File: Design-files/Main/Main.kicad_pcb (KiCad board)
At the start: 2 copper layers, 25 parts, among them J1 USB_B_Micro, J2 Conn_01x02_Pin, J3 Conn_01x24_Pin, J4 Conn_01x24_Socket, J5 Conn_01x24_Socket, J6 Conn_01x24_Pin, J7 Conn_01x10_Pin, U1 CH340C, U2 CAT24C256, U3 HT75xx-1-SOT89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

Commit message: changes
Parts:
- added C5: 1 uF, Capacitor_SMD:C_0201_0603Metric, F.Cu at (136.9, 52.9)
- added C6: 1 uF, Capacitor_SMD:C_0201_0603Metric, F.Cu at (136.9, 54.6)
- added C7: 10 uF, Capacitor_SMD:C_0201_0603Metric, F.Cu at (220.6, 55.9)
- added C8: 0.1uF, Capacitor_SMD:C_0201_0603Metric, F.Cu at (173.1, 116.8)
- added C9: 0.1uF, Capacitor_SMD:C_0201_0603Metric, F.Cu at (175.3, 99.1)
- added J13: Conn_01x02_Pin, Connector_PinHeader_2.54mm:PinHeader_1x02_P2.54mm_Vertical, F.Cu at (182.9, 68.6)
- added J8: Conn_01x04_Pin, Connector_PinHeader_2.54mm:PinHeader_1x04_P2.54mm_Vertical, F.Cu at (177.8, 68.6)
- added J9: Conn_01x02_Pin, Connector_PinHeader_2.54mm:PinHeader_1x02_P2.54mm_Vertical, F.Cu at (221.0, 68.6)
- added R10: 0, Resistor_SMD:R_0201_0603Metric, F.Cu at (141.8, 54.6)
- added R11: 10000, Resistor_SMD:R_0201_0603Metric, F.Cu at (217.4, 72.4)
- added R12: 10000, Resistor_SMD:R_0201_0603Metric, F.Cu at (237.2, 82.2)
- added R13: 0, Resistor_SMD:R_0201_0603Metric, F.Cu at (237.2, 84.0)
- added R14: 0, Resistor_SMD:R_0201_0603Metric, F.Cu at (241.0, 71.1)
- added R15: 0, Resistor_SMD:R_0201_0603Metric, F.Cu at (225.7, 91.4)
- added R16: 0, Resistor_SMD:R_0201_0603Metric, F.Cu at (141.8, 56.4)
- added R17: 0, Resistor_SMD:R_0201_0603Metric, F.Cu at (193.0, 108.4)
- added R18: 0, Resistor_SMD:R_0201_0603Metric, F.Cu at (210.7, 128.3)
- added R19: 4700, Resistor_SMD:R_0201_0603Metric, F.Cu at (203.5, 114.3)
- added R20: 4700, Resistor_SMD:R_0201_0603Metric, F.Cu at (218.4, 121.9)
- added R21: 0, Resistor_SMD:R_0201_0603Metric, F.Cu at (195.5, 108.4)
- added R22: 0, Resistor_SMD:R_0201_0603Metric, F.Cu at (213.2, 128.3)
- added R23: 0, Resistor_SMD:R_0201_0603Metric, F.Cu at (169.9, 96.5)
- added R24: 0, Resistor_SMD:R_0201_0603Metric, F.Cu at (197.9, 106.7)
- added R25: 0, Resistor_SMD:R_0201_0603Metric, F.Cu at (197.9, 108.4)
- added R26: 0, Resistor_SMD:R_0201_0603Metric, F.Cu at (215.6, 128.3)
- added R6: 0, Resistor_SMD:R_0201_0603Metric, F.Cu at (139.3, 54.6)
- added R7: 0, Resistor_SMD:R_0201_0603Metric, F.Cu at (139.3, 56.4)
- added R8: 0, Resistor_SMD:R_0201_0603Metric, F.Cu at (139.3, 58.1)
- added R9: 0, Resistor_SMD:R_0201_0603Metric, F.Cu at (141.8, 52.9)
- added U7: RT9073A, REG_RT9080-33GQZ:REG_RT9080-33GQZ, F.Cu at (158.3, 56.3)
- J2: value Conn_01x02_Pin -> Battery Jumper
- R2: value LDR03 -> 100K; footprint OptoDevice:R_LDR_10x8.5mm_P7.6mm_Vertical -> Resistor_SMD:R_0201_0603Metric
- R3: value 150K -> 100K
- Rprog1: value 2000 -> 1000
- U3: value HT75xx-1-SOT89 -> SHTC3; footprint Package_TO_SOT_SMD:SOT-89-3 -> Sensor_Humidity:Sensirion_DFN-4-1EP_2x2mm_P1mm_EP0.7x1.6mm
- moved U3 138.0 mm to (222.6, 58.9)
- moved R2 133.0 mm to (230.8, 58.4)
- moved U2 129.5 mm to (217.5, 132.2)
- moved R3 119.4 mm to (217.4, 70.6)
- moved J2 104.9 mm to (177.8, 50.8)
- moved U1 94.2 mm to (176.4, 90.8)
- moved J6 94.0 mm to (165.1, 68.6)
- moved J7 92.2 mm to (177.8, 104.1)
- moved Rprog1 78.4 mm to (141.8, 58.1)
- moved ChargingStatusLED1 78.1 mm to (158.5, 53.5)
- moved R5 77.2 mm to (139.3, 52.9)
- moved U4 76.4 mm to (145.6, 54.2)
- moved D1 76.4 mm to (152.2, 54.3)
- moved J5 75.1 mm to (154.9, 68.6)
- moved R1 72.6 mm to (136.9, 56.4)
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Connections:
- net AnalogueSensorOut renamed /BatterySense
- net DigitalSensorSCL renamed /DigitalSensorSCL
- net DigitalSensorSDA renamed /DigitalSensorSDA
- net EEPROMSCL renamed /Interfacing/EEPROMSCL
- net EEPROMSDA renamed /Interfacing/EEPROMSDA
- C2 pad 2: USB 5V -> Net-(ChargingStatusLED1-A)
- C3 pad 1: Battery Input Polarity Protection -> /Power Module/Battery Input Polarity Protection
- C4 pad 2: USB 5V -> Net-(U6-IN1)
- ChargingStatusLED1 pad 2: USB 5V -> Net-(ChargingStatusLED1-A)
- D1 pad 1: Battery Input Polarity Protection -> Net-(D1-K)
- J1 pad 1: USB 5V -> /USB 5V
- J1 pad 2: USB D- -> /Interfacing/USB D-
- J1 pad 3: USB D+ -> /Interfacing/USB D+
- J3 pad 11: USB 5V -> /USB 5V
- J3 pad 24: Regulated 3v3 -> /Regulated 3v3
- J4 pad 11: USB 5V -> /USB 5V
- J4 pad 24: Regulated 3v3 -> /Regulated 3v3
- J5 pad 6: USART_TX -> /Interfacing/USART_TX
- J5 pad 7: USART_RX -> /Interfacing/USART_RX
- J6 pad 6: USART_TX -> /Interfacing/USART_TX
- J6 pad 7: USART_RX -> /Interfacing/USART_RX
- J7 pad 1: Regulated 3v3 -> /Regulated 3v3
- J7 pad 7: USB 5V -> /USB 5V
- J7 pad 8: USART_TX -> /Interfacing/USART_TX
- J7 pad 9: USART_RX -> /Interfacing/USART_RX
- R3 pad 1: Regulated 3v3 -> Battery
- R4 pad 2: Switched Power -> Net-(U6-OUT)
- U1 pad 2: USART_RX -> Net-(U1-TXD)
- U1 pad 3: USART_TX -> Net-(U1-RXD)
- U1 pad 4: unconnected-(U1-V3-Pad4) -> Net-(U1-V3)
- U1 pad 5: USB D+ -> Net-(U1-UD+)
- U1 pad 6: USB D- -> Net-(U1-UD-)
- U3 pad 1: GND -> Net-(U3-VDD)
- U3 pad 2: Switched Power -> Net-(U3-SCL)
- U3 pad 3: Regulated 3v3 -> Net-(U3-SDA)
- U4 pad 3: Battery -> Net-(U4-BAT)
- U4 pad 4: USB 5V -> Net-(ChargingStatusLED1-A)
- U6 pad 6: Battery Input Polarity Protection -> /Power Module/Battery Input Polarity Protection
- U6 pad 7: Switched Power -> Net-(U6-OUT)
- U6 pad 8: USB 5V -> Net-(U6-IN1)
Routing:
- added copper zone on F.Cu, net GND

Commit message: lets go team
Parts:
- added R27: 0, Resistor_SMD:R_0201_0603Metric, F.Cu at (197.8, 55.9)
- R1, Rprog1: value 1000 -> 1k
- R11, R12: value 10000 -> 10k
- R19, R20: value 4700 -> 4.7k
- moved U6 2.54 mm to (125.9, 52.4)
- renumbered J3 to J3-Left1, J4 to J4-Left1, J5 to J5-Right1, J6 to J6-Right1
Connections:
- R3 pad 1: Battery -> Net-(R27-Pad1)

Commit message: hello
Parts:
- moved U6 72.3 mm to (193.7, 27.4)
- moved J7 70.3 mm to (120.2, 63.8), turned to 90 degrees
- moved C4 70.2 mm to (197.2, 26.7), turned to 90 degrees
- moved C3 68.7 mm to (197.2, 28.4), turned to 90 degrees
- moved C6 67.7 mm to (199.4, 28.6)
- moved C5 67.4 mm to (199.4, 27.6)
- moved C2 66.0 mm to (190.3, 19.6), turned to 180 degrees
- moved R4 64.5 mm to (194.9, 30.0), turned to 180 degrees
- moved C1 63.5 mm to (188.5, 19.6), turned to 180 degrees
- moved R9 63.3 mm to (199.4, 26.6)
- moved R7 60.7 mm to (194.8, 31.8), turned to 180 degrees
- moved R8 59.2 mm to (192.4, 31.8)
- moved R5 57.9 mm to (192.5, 30.0)
- moved R1 54.7 mm to (184.6, 29.7), turned to 90 degrees
- moved R6 54.5 mm to (184.7, 24.3), turned to 90 degrees
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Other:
- rule pad_to_mask_clearance: 0 -> 0.15

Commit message: lots of changes
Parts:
- removed C9: 0.1uF, Capacitor_SMD:C_0201_0603Metric
- removed R26: 0, Resistor_SMD:R_0201_0603Metric
- removed U2: CAT24C256, Package_TO_SOT_SMD:SOT-89-3
- added C10: 1 uF, footprint:C0402, F.Cu at (143.7, 58.4)
- added C11: 1 uF, footprint:C0402, F.Cu at (143.7, 64.5)
- added R28: 0, footprint:R0402, F.Cu at (147.8, 62.0)
- added U5: RT9073A-33GQZ, footprint:ZQFN-4L_L1.0-W1.0-P0.63-BL-EP, F.Cu at (143.6, 61.7)
- C1, C7: footprint Capacitor_SMD:C_0201_0603Metric -> footprint:C0603
- C2: footprint Capacitor_SMD:C_0201_0603Metric -> footprint:C0402
- C3, C4: footprint Capacitor_SMD:C_0201_0603Metric -> footprint:C1206
- C5, C6: value 1 uF -> 0.1uF; footprint Capacitor_SMD:C_0201_0603Metric -> footprint:C1206
- ChargingStatusLED1: footprint LED_SMD:LED_0805_2012Metric -> footprint:LED0805-RD
- D1: footprint Diode_SMD:D_SMA -> footprint:SMA_L4.2-W2.6-LS5.3-RD
- R1, Rprog1: footprint Resistor_SMD:R_0201_0603Metric -> footprint:R1206
- R10, R13, R14, R15, R16, R17, R18, R19, R20, R21, R22, R23, R24, R25, R27, R6, R7, R8, R9: footprint Resistor_SMD:R_0201_0603Metric -> footprint:R0402
- R11, R12: footprint Resistor_SMD:R_0201_0603Metric -> footprint:R0805
- R4: value 10K -> 700; footprint Resistor_SMD:R_0201_0603Metric -> footprint:R0603
- R5: value 700 -> 10K; footprint Resistor_SMD:R_0201_0603Metric -> footprint:R0805
- U1: footprint Package_SO:SOIC-8W_5.3x5.3mm_P1.27mm -> footprint:SOP-16_L10.0-W3.9-P1.27-LS6.0-BL
- U6: value TPS2115A-Q1 -> TPS2115ADRBR; footprint Package_TO_SOT_SMD:TSOT-23-8 -> footprint:SON-8_L3.0-W3.0-P0.65-LS3.0-BL-EP
- U7: value RT9073A -> M24C64-RMN6TP; footprint REG_RT9080-33GQZ:REG_RT9080-33GQZ -> footprint:SOIC-8_L5.0-W4.0-P1.27-LS6.0-BL
- moved R27 118.7 mm to (120.1, 63.3), turned to 180 degrees
- moved R2 114.5 mm to (116.8, 69.8), turned to 90 degrees
- moved C5 108.8 mm to (169.2, 132.1), turned to 180 degrees
- moved U7 107.4 mm to (142.9, 123.6), turned to -90 degrees
- moved C6 106.2 mm to (177.9, 132.6), turned to 180 degrees
- moved R9 96.1 mm to (169.2, 117.9), turned to 180 degrees
- moved R3 95.5 mm to (117.0, 75.7), turned to 180 degrees
- moved J2 82.6 mm to (120.4, 50.3)
- moved J1 80.8 mm to (146.1, 50.1), turned to 180 degrees
- moved R21 77.4 mm to (142.8, 128.0)
- moved J9 75.8 mm to (184.4, 100.1), turned to 180 degrees
- moved R13 75.7 mm to (170.4, 88.9)
- moved D1 72.6 mm to (128.5, 59.4), turned to 180 degrees
- moved C1 70.9 mm to (125.1, 51.3), turned to 0 degrees
- moved R16 70.3 mm to (120.2, 59.9), turned to 0 degrees
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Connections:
- C5 pad 1: /Power Module/Switched Power -> Net-(U1-V3)
- C6 pad 1: Net-(C6-Pad1) -> Net-(U1-VCC)
- R17 pad 2: Net-(U2-SDA) -> Net-(U7-SCL)
- R18 pad 2: Net-(U2-SCL) -> Net-(U7-SDA)
- R19 pad 1: Net-(U2-VCC) -> Net-(U7-VCC)
- R19 pad 2: Net-(U2-SDA) -> Net-(U7-SCL)
- R20 pad 1: Net-(U2-VCC) -> Net-(U7-VCC)
- R20 pad 2: Net-(U2-SCL) -> Net-(U7-SDA)
- R21 pad 2: Net-(U2-VCC) -> Net-(U7-VCC)
- R22 pad 1: /Interfacing/USART_RX -> Net-(U1-RXD)
- R22 pad 2: Net-(U1-TXD) -> /Interfacing/USART_TX
- R23 pad 1: Net-(U1-RXD) -> Net-(U1-D+)
- R23 pad 2: /Interfacing/USART_TX -> /Interfacing/USB D+
- R24 pad 1: Net-(U1-UD+) -> Net-(U1-D-)
- R24 pad 2: /Interfacing/USB D+ -> /Interfacing/USB D-
- R25 pad 1: Net-(U1-UD-) -> /Regulated 3v3
- R25 pad 2: /Interfacing/USB D- -> Net-(U1-VCC)
- R4 pad 1: GND -> Net-(U6-ILIM)
- R4 pad 2: Net-(U6-OUT) -> GND
- R5 pad 1: Net-(U6-ILIM) -> Net-(U6-STAT)
- R5 pad 2: GND -> Net-(U6-OUT)
- R7 pad 1: Net-(U6-OUT) -> Net-(U6-IN1)
- R7 pad 2: /Power Module/Switched Power -> /USB 5V
- R8 pad 1: Net-(U6-IN1) -> Net-(U6-OUT)
- R8 pad 2: /USB 5V -> /Power Module/Switched Power
- R9 pad 1: /Regulated 3v3 -> Net-(U1-TXD)
- R9 pad 2: Net-(C6-Pad1) -> /Interfacing/USART_RX
- U1 pad 5: Net-(U1-UD+) -> Net-(U1-D+)
- U1 pad 6: Net-(U1-UD-) -> Net-(U1-D-)
- U6 pad 1: GND -> Net-(U6-STAT)
- U6 pad 3: GND -> unconnected-(U6-D1-Pad3)
- U7 pad 1: Net-(C6-Pad1) -> GND
- U7 pad 3: /Power Module/Switched Power -> GND
- U7 pad 4: /Power Module/Switched Power -> GND
- U7 pad 5: Net-(C6-Pad1) -> Net-(U7-SDA)
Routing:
- net Battery: track 0.00 -> 38.8 mm
- net /BatterySense: track 0.00 -> 37.7 mm
- net Net-(U7-SDA): track 0.00 -> 35.5 mm
- net Net-(U7-VCC): track 0.00 -> 22.7 mm
- net /Interfacing/EEPROMSCL: track 0.00 -> 22.6 mm
- net /Interfacing/EEPROMSDA: track 0.00 -> 22.4 mm
- net /Regulated 3v3: track 0.00 -> 22.1 mm
- net Net-(U4-BAT): track 0.00 -> 15.9 mm
- net Net-(R27-Pad1): track 0.00 -> 13.7 mm
- net Net-(J3-Left1-Pin_9): track 0.00 -> 12.6 mm
- net Net-(J3-Left1-Pin_4): track 0.00 -> 12.6 mm
- net Net-(J3-Left1-Pin_20): track 0.00 -> 12.6 mm
- net Net-(J3-Left1-Pin_2): track 0.00 -> 12.6 mm
- net Net-(J3-Left1-Pin_18): track 0.00 -> 12.6 mm
- net Net-(J3-Left1-Pin_13): track 0.00 -> 12.6 mm
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
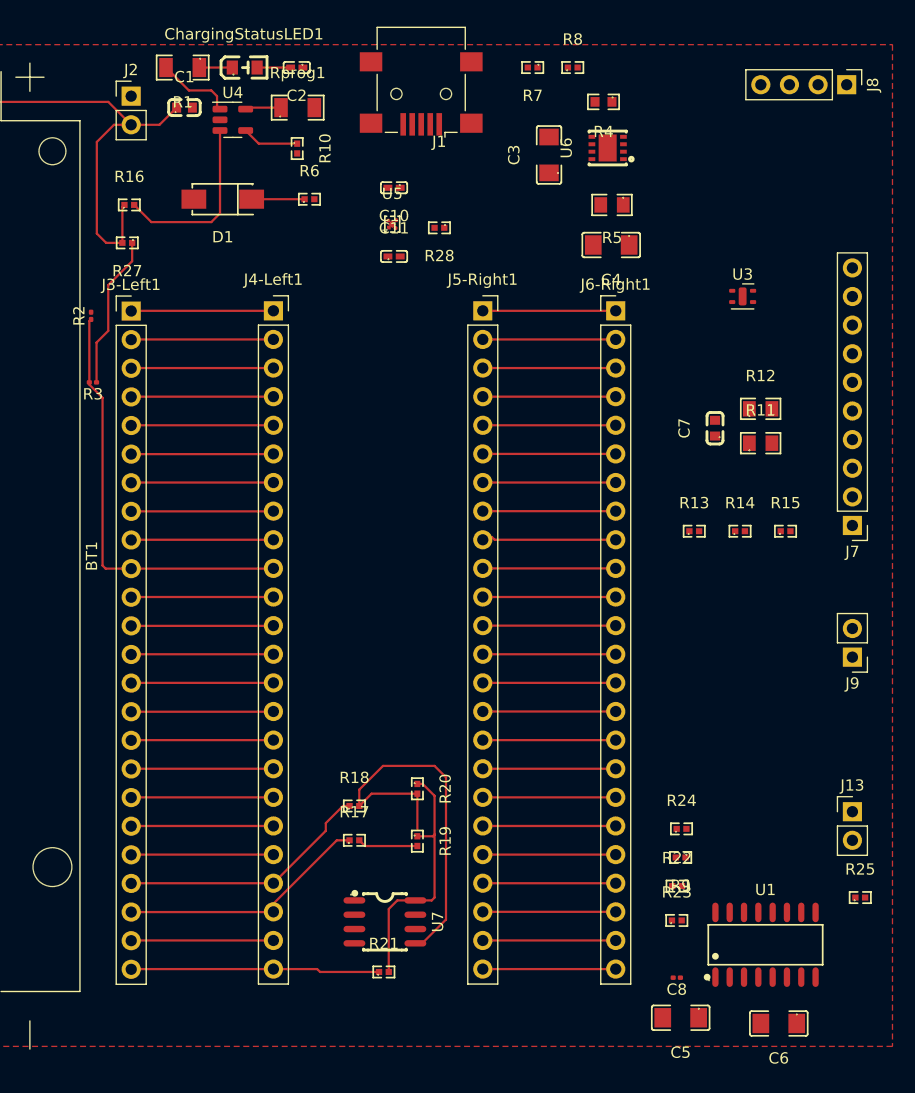
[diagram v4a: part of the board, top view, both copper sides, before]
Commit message: the labeling blocks added
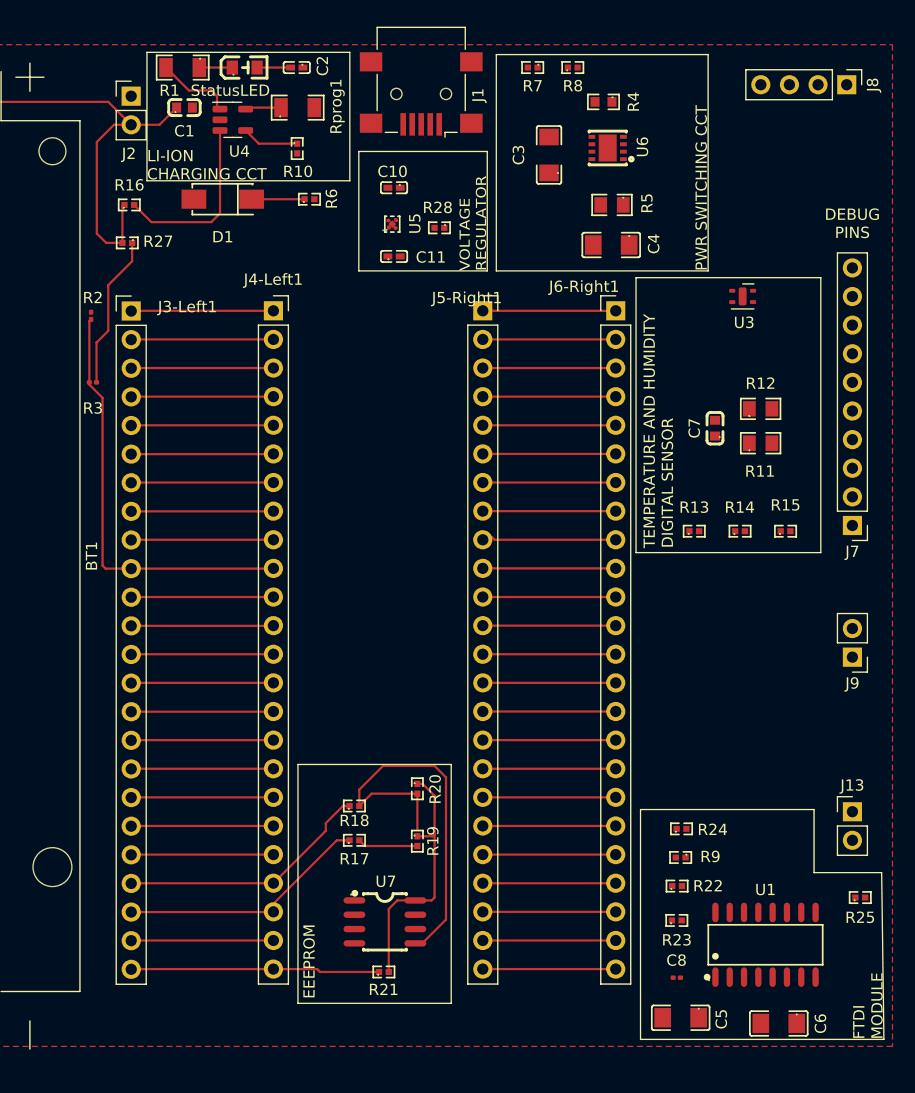
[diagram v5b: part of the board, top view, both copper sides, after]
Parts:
- renumbered ChargingStatusLED1 to StatusLED
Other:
- board text added: "DEBUG PINS"
- board text added: "EEEPROM"
- board text added: "FTDI MODULE"
- board text added: "LI-ION CHARGING CCT"
- board text added: "PWR SWITCHING CCT"
- board text added: "TEMPERATURE AND HUMIDITY DIGITAL SENSOR"
- board text added: "VOLTAGE REGULATOR"

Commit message: biggest change of my life
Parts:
- moved J1 80.6 mm to (142.2, 130.6), turned to 0 degrees
- moved R28 36.8 mm to (183.5, 53.3)
- moved C10 33.6 mm to (177.2, 55.2)
- moved C11 33.6 mm to (177.2, 61.3)
- moved U5 33.6 mm to (177.0, 58.4)
- moved J7 23.0 mm to (169.2, 71.1), turned to 0 degrees
- moved R8 17.6 mm to (170.6, 61.5)
- moved R23 16.0 mm to (184.7, 125.8), turned to 90 degrees
- moved C7 15.3 mm to (187.5, 81.5)
- moved R6 14.9 mm to (144.9, 47.2)
- moved R7 14.3 mm to (154.5, 61.9)
- moved R16 14.1 mm to (134.2, 58.0)
- moved C3 11.5 mm to (168.8, 53.0), turned to -90 degrees
- moved D1 11.0 mm to (119.8, 52.6), turned to 90 degrees
- moved R3 9.72 mm to (118.2, 66.0)
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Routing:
- net /USB 5V: track 12.6 -> 253.6 mm
- net /Regulated 3v3: track 22.1 -> 200.2 mm
- net /DigitalSensorSDA: track 12.6 -> 91.2 mm
- net /BatterySense: track 37.7 -> 110.1 mm
- net /Interfacing/USB D-: track 0.00 -> 68.3 mm, vias 0 -> 1
- net /DigitalSensorSCL: track 12.6 -> 74.9 mm
- net /Interfacing/USB D+: track 0.00 -> 61.5 mm, vias 0 -> 2
- net /Power Module/Battery Input Polarity Protection: track 0.00 -> 51.1 mm
- net /Interfacing/USART_TX: track 11.8 -> 51.2 mm
- net /Interfacing/USART_RX: track 11.8 -> 45.3 mm
- net Net-(U1-VCC): track 0.00 -> 31.1 mm
- net Net-(U3-SCL): track 0.00 -> 30.8 mm
- net Net-(D1-K): track 4.70 -> 31.7 mm
- net Net-(U6-OUT): track 0.00 -> 26.6 mm, vias 0 -> 2
- net Net-(U3-SDA): track 0.00 -> 25.4 mm
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- added copper zone on B.Cu, net GND
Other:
- board text added: "Battery Connect"

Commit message: changes
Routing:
- net /Regulated 3v3: track 200.2 -> 280.9 mm
- net /Power Module/Battery Input Polarity Protection: track 51.1 -> 84.2 mm
- net /Power Module/Switched Power: track 22.6 -> 49.3 mm
- net Battery: track 43.1 -> 64.4 mm
- net /USB 5V: track 253.6 -> 270.9 mm
- net Net-(U1-VCC): track 31.1 -> 47.1 mm
- net /BatterySense: track 110.1 -> 123.3 mm
- net Net-(U1-V3): track 11.1 -> 21.8 mm
- net Net-(U6-IN1): track 9.73 -> 19.1 mm
- net Net-(ChargingStatusLED1-A): track 17.3 -> 26.4 mm
- net Net-(U4-BAT): track 7.83 -> 16.3 mm
- net Net-(U6-OUT): track 26.6 -> 19.1 mm
- net Net-(U6-STAT): track 4.05 -> 8.12 mm
- net Net-(U3-VDD): track 24.1 -> 27.9 mm
- net Net-(R27-Pad1): track 9.09 -> 7.26 mm
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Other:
- board outline added: 99.5 x 90.4 mm

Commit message: fixed shematic
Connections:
- C2 pad 2: Net-(ChargingStatusLED1-A) -> Net-(#FLG06-pwr)
- R10 pad 1: Net-(ChargingStatusLED1-A) -> Net-(#FLG06-pwr)
- U4 pad 4: Net-(ChargingStatusLED1-A) -> Net-(#FLG06-pwr)
- U5 pad 3: Net-(U5-EN) -> /Power Module/Switched Power
- U5 pad 4: Net-(U5-VIN) -> /Power Module/Switched Power
- U5 pad 5: Net-(U5-EN) -> GND
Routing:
- net Net-(ChargingStatusLED1-A): track 26.4 -> 0.00 mm
- net Net-(#FLG06-pwr): track 0.00 -> 15.0 mm
- net /Power Module/Switched Power: track 49.3 -> 62.7 mm
- net Net-(U5-EN): track 3.53 -> 0.00 mm
- net Net-(U5-VIN): track 2.94 -> 0.00 mm
- net Net-(U5-VOUT): track 16.6 -> 19.4 mm
- net GND: track 3.84 -> 5.20 mm
